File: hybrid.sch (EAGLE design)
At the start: 59 parts, among them J1 RCJ-21XXMILL, J3 NRJ3HF-1, Q1 BC560KINKED, Q10 BC550KINKED, Q11 BC550KINKED, Q12 BC560KINKED, Q13 BD140, Q14 BD139, Q2 BC556KINKED, Q3 BC550KINKED, Q4 BC550KINKED, Q5 BC560KINKED, Q6 BD140, Q7 BD139, Q8 BC560KINKED, Q9 BC556KINKED

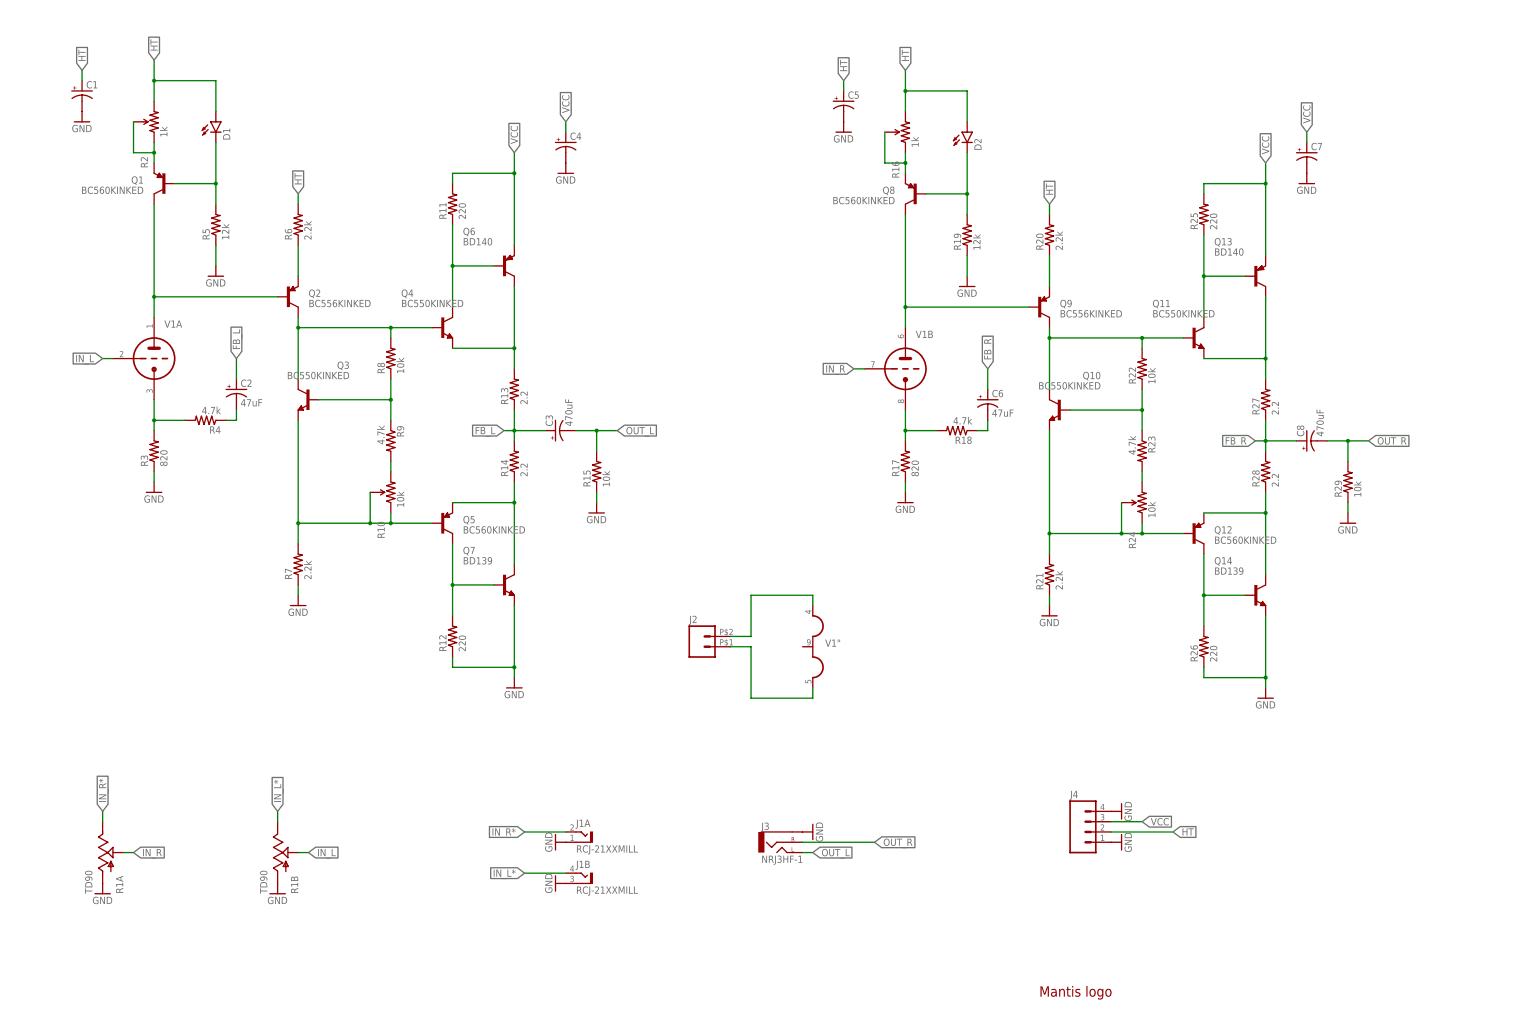
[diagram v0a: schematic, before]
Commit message: Mounting holes, caps layout
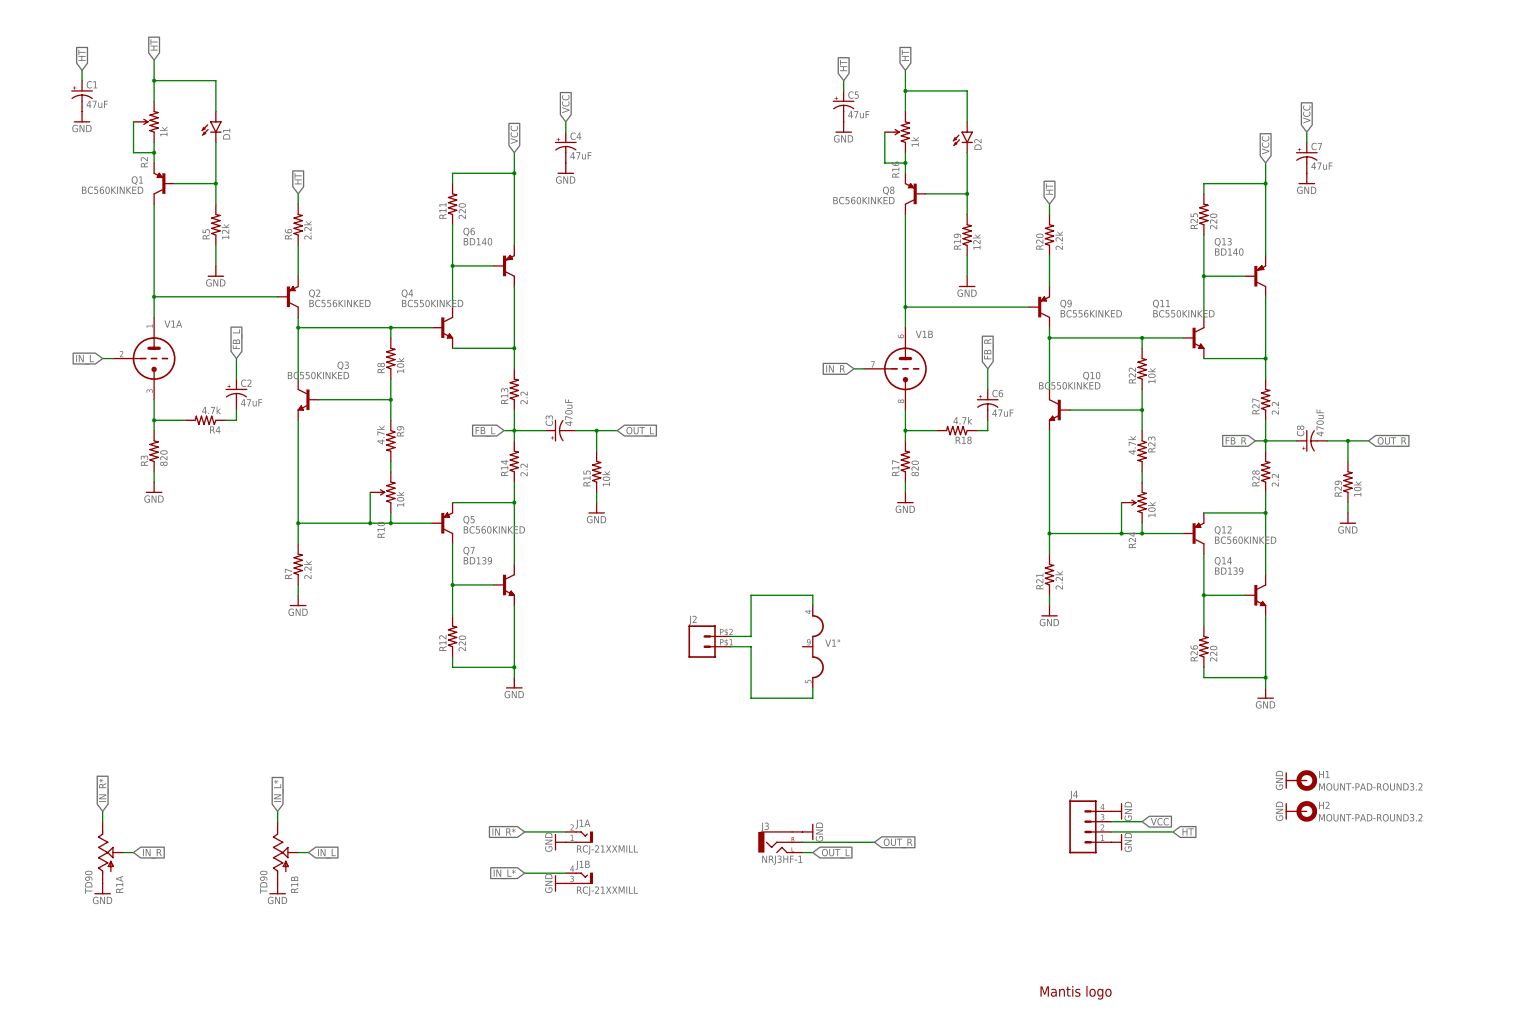
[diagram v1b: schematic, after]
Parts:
- added H1, H2: MOUNT-PAD-ROUND3.2, holes:MOUNT-PAD-ROUND3.2
- C1, C4, C5, C7: value (none) -> 47uF; device my-cap:CAP_POLPTH1 -> my-cap:CAP_POLPTH-8/3.5
- C2, C6: device my-cap:CAP_POLPTH4 -> my-cap:CAP_POLPTH-8/3.5
- C3, C8: device my-cap:CAP_POLPTH3 -> my-cap:CAP_POLPTH-16/7.5
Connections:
- net GND: now also H1.MOUNT, H2.MOUNT
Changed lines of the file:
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@@
 <part name="R4" library="SparkFun-Resistors" deviceset="RESISTOR" device="PTH-1/4W" value="4.7k"/>
 <part name="GND3" library="SparkFun-Aesthetics" deviceset="GND" device=""/>
-<part name="C2" library="my-cap" deviceset="CAP_POL" device="PTH4" value="47uF"/>
+<part name="C2" library="my-cap" deviceset="CAP_POL" device="PTH-8/3.5" value="47uF"/>
 <part name="Q2" library="my-tran" deviceset="BC556" device="KINKED"/>
 <part name="R6" library="SparkFun-Resistors" deviceset="RESISTOR" device="PTH-1/4W" value="2.2k"/>
@@
 <part name="R12" library="SparkFun-Resistors" deviceset="RESISTOR" device="PTH-1/4W" value="220"/>
 <part name="GND7" library="SparkFun-Aesthetics" deviceset="GND" device=""/>
-<part name="C3" library="my-cap" deviceset="CAP_POL" device="PTH3" value="470uF"/>
+<part name="C3" library="my-cap" deviceset="CAP_POL" device="PTH-16/7.5" value="470uF"/>
 <part name="R15" library="SparkFun-Resistors" deviceset="RESISTOR" device="PTH-1/4W" value="10k"/>
 <part name="GND11" library="SparkFun-Aesthetics" deviceset="GND" device=""/>
@@
 <part name="R18" library="SparkFun-Resistors" deviceset="RESISTOR" device="PTH-1/4W" value="4.7k"/>
 <part name="GND14" library="SparkFun-Aesthetics" deviceset="GND" device=""/>
-<part name="C6" library="my-cap" deviceset="CAP_POL" device="PTH4" value="47uF"/>
+<part name="C6" library="my-cap" deviceset="CAP_POL" device="PTH-8/3.5" value="47uF"/>
 <part name="Q9" library="my-tran" deviceset="BC556" device="KINKED"/>
 <part name="R20" library="SparkFun-Resistors" deviceset="RESISTOR" device="PTH-1/4W" value="2.2k"/>
@@
 <part name="R26" library="SparkFun-Resistors" deviceset="RESISTOR" device="PTH-1/4W" value="220"/>
 <part name="GND19" library="SparkFun-Aesthetics" deviceset="GND" device=""/>
-<part name="C8" library="my-cap" deviceset="CAP_POL" device="PTH3" value="470uF"/>
+<part name="C8" library="my-cap" deviceset="CAP_POL" device="PTH-16/7.5" value="470uF"/>
 <part name="R29" library="SparkFun-Resistors" deviceset="RESISTOR" device="PTH-1/4W" value="10k"/>
 <part name="GND21" library="SparkFun-Aesthetics" deviceset="GND" device=""/>
@@
 <part name="GND9" library="SparkFun-Aesthetics" deviceset="GND" device=""/>
 <part name="GND8" library="SparkFun-Aesthetics" deviceset="GND" device=""/>
-<part name="C4" library="my-cap" deviceset="CAP_POL" device="PTH1"/>
+<part name="C4" library="my-cap" deviceset="CAP_POL" device="PTH-8/3.5" value="47uF"/>
 <part name="GND10" library="SparkFun-Aesthetics" deviceset="GND" device=""/>
-<part name="C7" library="my-cap" deviceset="CAP_POL" device="PTH1"/>
+<part name="C7" library="my-cap" deviceset="CAP_POL" device="PTH-8/3.5" value="47uF"/>
 <part name="GND20" library="SparkFun-Aesthetics" deviceset="GND" device=""/>
-<part name="C1" library="my-cap" deviceset="CAP_POL" device="PTH1"/>
+<part name="C1" library="my-cap" deviceset="CAP_POL" device="PTH-8/3.5" value="47uF"/>
 <part name="GND1" library="SparkFun-Aesthetics" deviceset="GND" device=""/>
-<part name="C5" library="my-cap" deviceset="CAP_POL" device="PTH1"/>
+<part name="C5" library="my-cap" deviceset="CAP_POL" device="PTH-8/3.5" value="47uF"/>
 <part name="GND13" library="SparkFun-Aesthetics" deviceset="GND" device=""/>
 <part name="GND12" library="SparkFun-Aesthetics" deviceset="GND" device=""/>
@@
 <part name="GND18" library="SparkFun-Aesthetics" deviceset="GND" device=""/>
 <part name="LOGO1" library="my" deviceset="LOGO-MANTIS" device=""/>
+<part name="H1" library="holes" deviceset="MOUNT-PAD-ROUND" device="3.2"/>
+<part name="H2" library="holes" deviceset="MOUNT-PAD-ROUND" device="3.2"/>
+<part name="GND22" library="SparkFun-Aesthetics" deviceset="GND" device=""/>
+<part name="GND23" library="SparkFun-Aesthetics" deviceset="GND" device=""/>
 </parts>
 <sheets>
@@
 <instance part="GND18" gate="1" x="281.94" y="45.72" rot="R90"/>
 <instance part="LOGO1" gate="G$1" x="271.78" y="7.62"/>
+<instance part="H1" gate="G$1" x="327.66" y="60.96"/>
+<instance part="H2" gate="G$1" x="327.66" y="53.34"/>
+<instance part="GND22" gate="1" x="322.58" y="60.96" rot="R270"/>
+<instance part="GND23" gate="1" x="322.58" y="53.34" rot="R270"/>
 </instances>
 <busses>
@@
 <pinref part="GND18" gate="1" pin="GND"/>
 </segment>
+<segment>
+<pinref part="H1" gate="G$1" pin="MOUNT"/>
+<pinref part="GND22" gate="1" pin="GND"/>
+</segment>
+<segment>
+<pinref part="H2" gate="G$1" pin="MOUNT"/>
+<pinref part="GND23" gate="1" pin="GND"/>
+</segment>
 </net>

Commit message: Amp + PS on the same board. Rerouted from scratch
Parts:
- removed J3: NRJ3HF-1, my-conn:NRJ3HF-1
- removed J4: (no value), SparkFun-Connectors:M04POLAR
- added A1: R-78HBXX-0.5, my-smps:R-78HBXX-0.5
- added C10, C12, C26, C27, C9: 47uF, my-cap:CAP_POLPTH-8/3.5
- added C11: 10p, SparkFun-Capacitors:CAPPTH
- added C13, C14: 470uF, my-cap:CAP_POLPTH-12/5
- added C15, C16: 470uF, my-cap:CAP_POLPTH-16/7.5
- added C18: 4700uF, my-cap:CAP_POLPTH-22/10
- added C19, C24, C25: 1uF, SparkFun-Capacitors:CAPPTH
- added C21: 47uF, my-cap:CAP_POLPTH-12/5
- added C22: 10uF, my-cap:CAP_POLPTH-5/2.5
- added C23: 10uF, my-cap:CAP_POLPTH-6.5/2.5
- added D10, D11, D12, D3, D4, D5, D6, D7, D8, D9: (no value), SparkFun-DiscreteSemi:DIODEPTH
- added GB1: COPPER-BRIDGESM, my:COPPER-BRIDGESM
- added H3: MOUNT-HOLE3.2, holes:MOUNT-HOLE3.2
- added IC1, IC2: LM317MABT, v-reg:LM317MABT
- added PAD1: 30VAC_H, wirepad:3,81/1,4
- added PAD2: 30VAC_L, wirepad:3,81/1,4
- added Q15: KSP43, my-tran:KSP43
- added R30: 2.2, SparkFun-Resistors:RESISTORPTH-1/2W
- added R31: 10k, SparkFun-Resistors:RESISTORPTH-1/4W
- added R32: 0.536, my-res:RESISTORPTH-1/2W
- added R33: 2.2k, SparkFun-Resistors:RESISTORPTH-1/4W
- added R34: 240, SparkFun-Resistors:RESISTORPTH-1/4W
- added R35: 5.49k, SparkFun-Resistors:RESISTORPTH-1/4W
- added R36: 510, SparkFun-Resistors:RESISTORPTH-1/4W
- added R37: 23.7k, SparkFun-Resistors:RESISTORPTH-1/4W
- C1: value 47uF -> 0.47u; device my-cap:CAP_POLPTH-8/3.5 -> capacitor-wima:C5/3.5
- C3: value 470uF -> 47uF; device my-cap:CAP_POLPTH-16/7.5 -> my-cap:CAP_POLPTH-8/3.5
- C4: value 47uF -> 10p; device my-cap:CAP_POLPTH-8/3.5 -> SparkFun-Capacitors:CAPPTH
- C6, C7: value 47uF -> 470uF; device my-cap:CAP_POLPTH-8/3.5 -> my-cap:CAP_POLPTH-12/5
- C8: value 470uF -> 0.47u; device my-cap:CAP_POLPTH-16/7.5 -> capacitor-wima:C5/3.5
- H2: value MOUNT-PAD-ROUND3.2 -> MOUNT-HOLE3.2; device holes:MOUNT-PAD-ROUND3.2 -> holes:MOUNT-HOLE3.2
- J2: value (none) -> NRJ3HF-1; device SparkFun-Connectors:M02PTH2 -> my-conn:NRJ3HF-1
- R1: value TD90 -> 1Meg; device my:TD90 -> SparkFun-Resistors:RESISTORPTH-1/4W
- R10: value 10k -> 4.7k; device SparkFun-Electromechanical:TRIMPOT3362U-2 -> SparkFun-Resistors:RESISTORPTH-1/4W
- R11, R26: value 220 -> 10k; device SparkFun-Resistors:RESISTORPTH-1/4W -> SparkFun-Electromechanical:TRIMPOT3362U-2
- R13, R27, R28: value 2.2 -> 220; device SparkFun-Resistors:RESISTORPTH-1/2W -> SparkFun-Resistors:RESISTORPTH-1/4W
- R15, R29: value 10k -> 2.2; device SparkFun-Resistors:RESISTORPTH-1/4W -> SparkFun-Resistors:RESISTORPTH-1/2W
- R16: value 1k -> 10k; device SparkFun-Electromechanical:TRIMPOT3362U-2 -> SparkFun-Resistors:RESISTORPTH-1/4W
- R17: value 820 -> 1Meg
- R18: value 4.7k -> 1k; device SparkFun-Resistors:RESISTORPTH-1/4W -> SparkFun-Electromechanical:TRIMPOT3362U-2
- R19: value 12k -> 820
- R2: value 1k -> TD90; device SparkFun-Electromechanical:TRIMPOT3362U-2 -> my:TD90
- R20: value 2.2k -> 4.7k
- R21, R6: value 2.2k -> 12k
- R22, R8: value 10k -> 2.2k
- R23: value 4.7k -> 2.2k
- R24: device SparkFun-Electromechanical:TRIMPOT3362U-2 -> SparkFun-Resistors:RESISTORPTH-1/4W
- R25: value 220 -> 4.7k
- R3: value 820 -> 1k; device SparkFun-Resistors:RESISTORPTH-1/4W -> SparkFun-Electromechanical:TRIMPOT3362U-2
- R4: value 4.7k -> 820
- R5: value 12k -> 4.7k
- R9: value 4.7k -> 10k
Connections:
- removed net N$1: J2.2, V1".H1
- removed net N$6: J2.1, V1".H3
- new net +6.3FIL: R32.2, V1".H1
- new net +LV: A1.IN, C18.+, D10.C, D7.C, D8.C, IC1.IN
- new net 30VAC_H: C15.-, D4.C, D7.A, PAD1.P
- new net 30VAC_L: D3.A, D5.C, D8.A, PAD2.P
- new net N$18: C8.2, R17.2, V1B.TG
- new net N$30: C22.+, C24.1, D11.A, IC1.ADJ, R34.2, R35.1
- new net N$31: C15.+, D3.C, D6.A
- new net N$32: A1.OUT, R32.1
- new net N$33: C16.+, D6.C, D9.C, Q15.C, R33.1
- new net N$34: C19.1, C21.+, Q15.B, R33.2
- new net N$36: C23.+, C25.1, D12.A, IC2.ADJ, R36.2, R37.1
- new net N$37: IC2.IN, Q15.E
- new net N$9: C1.2, R1.2, V1A.TG
- new net SGND: GB1.2, V1".H3
- net CAT_L: now also R5.2; no longer R3.2
- net CAT_R: now also R19.2, R20.2; no longer R17.2, R18.2
- net FB_L: now also C6.+, C7.+, R14.1, R15.2; no longer C2.+, C3.+, R13.1, R14.2
- net FB_R: now also C13.+, C14.+, R29.1, R30.2; no longer C6.+, C8.+, R27.1, R28.2
- net GND: now also A1.GND, C12.-, C16.-, C18.-, C19.2, C2.-, C21.-, C22.-, C23.-, C24.2, C25.2, C26.-, C27.-, C9.-, D4.A, D5.A, GB1.1, J2.SLEEVE, R1.1, R13.1, R16.1, R23.1, R28.1, R2A.A, R2B.A, R31.1, R35.2, R37.2, R4.1, R6.1, R8.1; no longer C1.-, C4.-, C7.-, H2.MOUNT, J3.SLEEVE, J4.1, J4.4, R12.1, R15.1, R1A.A, R1B.A, R26.1, R29.1, R3.1, R5.1, R7.1
- net HT: now also C2.+, C27.+, C9.+, D12.C, D9.A, IC2.OUT, R18.CW, R22.2, R3.CW, R36.1, R7.2; no longer C1.+, C5.+, J4.2, R16.CW, R2.CW, R20.2, R6.2
- net IN_L: now also C1.1, R2B.S; no longer R1B.S, V1A.TG
- net IN_L*: now also R2B.E; no longer R1B.E
- net IN_R: now also C8.1, R2A.S; no longer R1A.S, V1B.TG
- net IN_R*: now also R2A.E; no longer R1A.E
- net N$10: now also R10.2, R11.CW; no longer R10.CW, R9.2
- net N$11: now also R14.2; no longer R13.2
- net N$12: now also R11.CCW, R11.WIPER, R8.2; no longer R10.CCW, R10.WIPER, R7.2
- net N$13: now also R15.1; no longer R14.1
- net N$14: now also R12.1; no longer R11.1
- net N$15: now also R13.2; no longer R12.2
- net N$16: now also R18.CCW, R18.WIPER; no longer R16.CCW, R16.WIPER
- net N$17: now also R21.2; no longer R19.2
- net N$19: now also C10.+, R20.1; no longer C6.-, R18.1
- net N$2: now also R3.CCW, R3.WIPER; no longer R2.CCW, R2.WIPER
- net N$20: now also R22.1; no longer R20.1
- net N$21: now also C11.2, R24.2; no longer R22.2
- net N$22: now also R24.1, R25.1; no longer R22.1, R23.1
- net N$23: now also R25.2, R26.CW; no longer R23.2, R24.CW
- net N$24: now also R23.2, R26.CCW, R26.WIPER; no longer R21.2, R24.CCW, R24.WIPER
- net N$25: now also R29.2; no longer R27.2
- net N$26: now also R30.1; no longer R28.1
- net N$27: now also R27.1; no longer R25.1
- net N$28: now also R28.2; no longer R26.2
- net N$3: now also R6.2; no longer R5.2
- net N$4: now also C3.+, R5.1; no longer C2.-, R4.1
- net N$5: now also R7.1; no longer R6.1
- net N$7: now also C4.2, R9.2; no longer R8.2
- net N$8: now also R10.1; no longer R8.1
- net OUT_L: now also C6.-, C7.-, J2.LEFT, R16.2; no longer J3.LEFT, R15.2
- net OUT_R: now also C10.-, C13.-, C14.-, J2.RIGHT, R31.2; no longer C8.-, J3.RIGHT, R29.2
- net PL_L: now also C4.1
- net PL_R: now also C11.1
- net VCC: now also C12.+, C26.+, C5.+, D10.A, D11.C, IC1.OUT, R12.2, R27.2, R34.1; no longer C4.+, C7.+, J4.3, R11.2, R25.2

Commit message: Small fix
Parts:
- R21, R6: value 12k -> 33k
- R32: value 0.536 -> 0.549
- V1: value (none) -> 6DJ8
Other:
- note added: "1.7V"
- note added: "45V"
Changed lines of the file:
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@@
 </classes>
 <parts>
-<part name="V1" library="tubes" deviceset="6DJ8-P" device=""/>
+<part name="V1" library="tubes" deviceset="6DJ8-P" device="" value="6DJ8"/>
 <part name="Q1" library="my-tran" deviceset="BC560" device="KINKED"/>
 <part name="R3" library="SparkFun-Electromechanical" deviceset="TRIMPOT" device="3362U-2" value="1k"/>
 <part name="D1" library="SparkFun-LED" deviceset="LED" device="3MM"/>
-<part name="R6" library="SparkFun-Resistors" deviceset="RESISTOR" device="PTH-1/4W" value="12k"/>
+<part name="R6" library="SparkFun-Resistors" deviceset="RESISTOR" device="PTH-1/4W" value="33k"/>
 <part name="GND5" library="SparkFun-Aesthetics" deviceset="GND" device=""/>
 <part name="R4" library="SparkFun-Resistors" deviceset="RESISTOR" device="PTH-1/4W" value="820"/>
@@
 <part name="R18" library="SparkFun-Electromechanical" deviceset="TRIMPOT" device="3362U-2" value="1k"/>
 <part name="D2" library="SparkFun-LED" deviceset="LED" device="3MM"/>
-<part name="R21" library="SparkFun-Resistors" deviceset="RESISTOR" device="PTH-1/4W" value="12k"/>
+<part name="R21" library="SparkFun-Resistors" deviceset="RESISTOR" device="PTH-1/4W" value="33k"/>
 <part name="GND18" library="SparkFun-Aesthetics" deviceset="GND" device=""/>
 <part name="R19" library="SparkFun-Resistors" deviceset="RESISTOR" device="PTH-1/4W" value="820"/>
@@
 <part name="A1" library="my-smps" deviceset="R-78HBXX-0.5" device=""/>
 <part name="GND27" library="SparkFun-Aesthetics" deviceset="GND" device=""/>
-<part name="R32" library="my-res" deviceset="RESISTOR" device="PTH-1/2W" value="0.536"/>
+<part name="R32" library="my-res" deviceset="RESISTOR" device="PTH-1/2W" value="0.549"/>
 <part name="GB1" library="my" deviceset="COPPER-BRIDGE" device="SM" value=""/>
 <part name="GND35" library="SparkFun-Aesthetics" deviceset="GND" device=""/>
@@
 <sheet>
 <plain>
+<text x="66.04" y="226.06" size="1.778" layer="97">1.7V</text>
+<text x="33.02" y="185.42" size="1.778" layer="97">45V</text>
 </plain>
 <instances>

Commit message: Small fix
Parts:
- R16, R31: value 10k -> 2.2k
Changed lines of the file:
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@@
 <part name="GND8" library="SparkFun-Aesthetics" deviceset="GND" device=""/>
 <part name="C7" library="my-cap" deviceset="CAP_POL" device="PTH-12/5" value="470uF"/>
-<part name="R16" library="SparkFun-Resistors" deviceset="RESISTOR" device="PTH-1/4W" value="10k"/>
+<part name="R16" library="SparkFun-Resistors" deviceset="RESISTOR" device="PTH-1/4W" value="2.2k"/>
 <part name="GND12" library="SparkFun-Aesthetics" deviceset="GND" device=""/>
 <part name="Q8" library="my-tran" deviceset="BC560" device="KINKED"/>
@@
 <part name="GND20" library="SparkFun-Aesthetics" deviceset="GND" device=""/>
 <part name="C14" library="my-cap" deviceset="CAP_POL" device="PTH-12/5" value="470uF"/>
-<part name="R31" library="SparkFun-Resistors" deviceset="RESISTOR" device="PTH-1/4W" value="10k"/>
+<part name="R31" library="SparkFun-Resistors" deviceset="RESISTOR" device="PTH-1/4W" value="2.2k"/>
 <part name="GND24" library="SparkFun-Aesthetics" deviceset="GND" device=""/>
 <part name="J2" library="my-conn" deviceset="NRJ3HF-1" device=""/>
